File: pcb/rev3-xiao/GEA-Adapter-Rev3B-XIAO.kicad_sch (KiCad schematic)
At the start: 19 parts, among them J1 CURRENT_LIMITED_5V_IN, J2 GEA3_UART, U2 XIAO-ESP32-C3-SMD, U3 74LVC2G07

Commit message: feat(pcb): add rev3b appliance power path
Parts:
- removed J1: CURRENT_LIMITED_5V_IN, Connector_PinHeader_2.54mm:PinHeader_1x02_P2.54mm_Vertical, symbol Connector_Generic:Conn_01x02
- removed J2: GEA3_UART, Connector_PinHeader_2.54mm:PinHeader_1x02_P2.54mm_Vertical, symbol Connector_Generic:Conn_01x02
- added C10, C15: 100n 50V X7R, Capacitor_SMD:C_0603_1608Metric, symbol Device:C
- added C16, C17: 22u 16V X8L, Capacitor_SMD:C_1210_3225Metric, symbol Device:C
- added C8: 1u, Capacitor_SMD:C_0805_2012Metric, symbol Device:C
- added C9: 10u 50V X7R, Capacitor_SMD:C_1206_3216Metric, symbol Device:C
- added D12, D13: BZX84C12LT1G, Package_TO_SOT_SMD:SOT-23, symbol Diode:BZX84Cxx
- added D7: DNI, Diode_SMD:D_SMA, symbol Device:D_TVS
- added F1, F2: Polyfuse, Fuse:Fuse_1812_4532Metric, symbol Device:Polyfuse
- added J1: 8P8C, Connector_RJ:RJ45_Amphenol_54602-x08_Horizontal, symbol Connector:8P8C
- added JP2: APPLIANCE PIN 1 / PIN 3, Connector_PinHeader_2.54mm:PinHeader_1x03_P2.54mm_Vertical, symbol GEA:JP_PWR_3PIN
- added L1: 4.7uH, Inductor_SMD:L_Panasonic_PCC-M0530M, symbol Device:L
- added Q1, Q2: Si2309CDS, Package_TO_SOT_SMD:SOT-23, symbol Device:Q_PMOS_GSD
- added R30, R9: 9.1k, Resistor_SMD:R_0805_2012Metric, symbol Device:R
- added R8: DNP, Resistor_SMD:R_0805_2012Metric, symbol Device:R
- added U8: AP63205WU, Package_TO_SOT_SMD:TSOT-23-6, symbol Regulator_Switching:AP63205WU
- U2: LCSC/JLCPCB (none) -> C18212168
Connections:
- net APPL_5V: now also C16.1, C17.1, L1.2, U8.1 (FB)
- net GEA3_APPL_RX: now also J1.4
- net GEA3_APPL_TX: now also J1.5
- net GND: now also C10.1, C16.2, C17.2, C9.2, D7.1 (A1), J1.8, R30.2, R9.1, U8.4 (GND)
- new net ALT_PWR: F1.1, J1.3
- new net APPLIANCE_PROTECTED: C10.2, C9.1, Q2.3 (D), U8.2 (EN), U8.3 (IN)
- new net BUCK_BST: C15.1, U8.6 (BST)
- new net BUCK_SW: C15.2, L1.1, U8.5 (SW)
- new net PIN1_FUSED: F2.2, JP2.1 (RUN)
- new net PIN3_FUSED: F1.2, JP2.3 (NC_PARK)
- new net PWR_PROTECT_MID: C8.1, D12.3 (K), D13.3 (K), Q1.2 (S), Q2.2 (S), R8.2
- new net PWR_SELECTED: D7.2 (A2), JP2.2 (XIAO_5V), Q1.3 (D)
- new net Q1_GATE: D12.1 (A), Q1.1 (G), R30.1
- new net Q2_GATE: C8.2, D13.1 (A), Q2.1 (G), R8.1, R9.2
- new net VDC: F2.1, J1.1
- no-connect marks 16 -> 19
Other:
- note added: "JP2: appliance input selector. Shunt 1-2 selects RJ45 pin 1 VDC; shunt 2-3 selects pin 3 ALT_PWR. Move only with power off."
- note added: "JP_PWR is separate: RUN bridges appliance-regulated 5 V to XIAO VBUS; USB DEBUG parks the shunt and isolates appliance power."

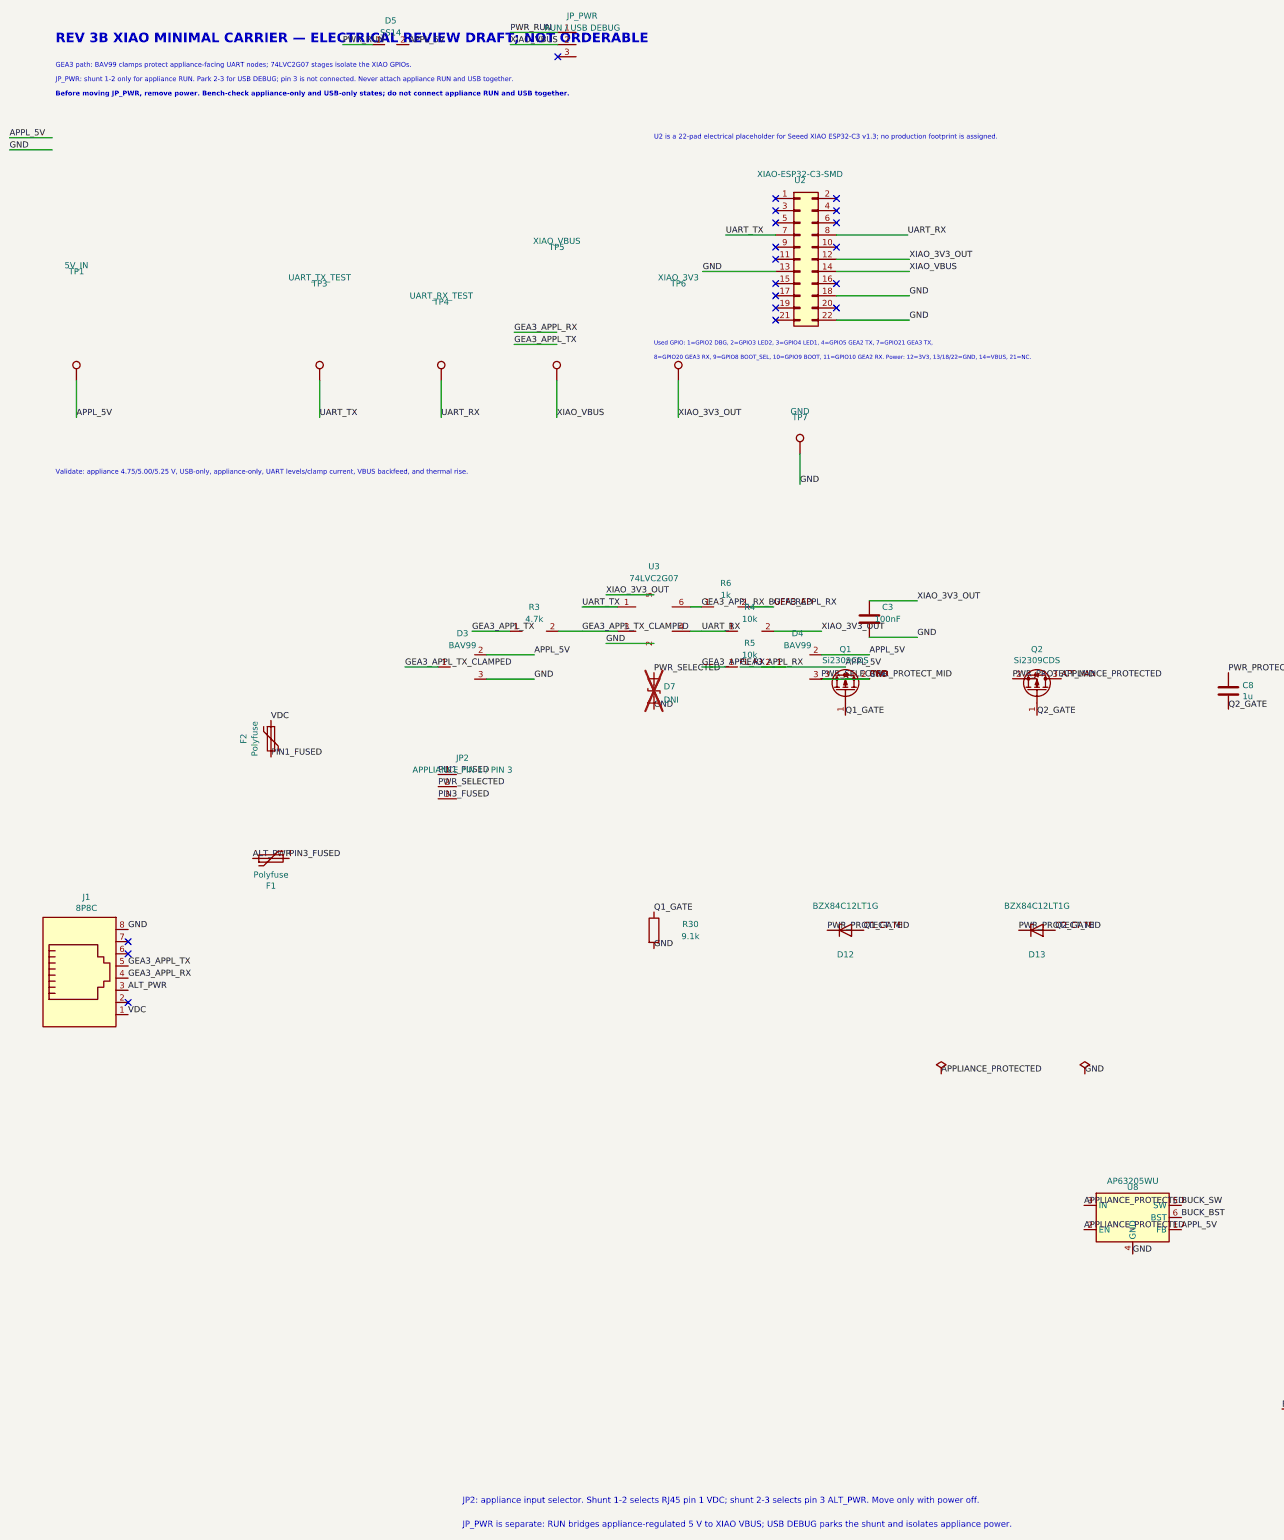
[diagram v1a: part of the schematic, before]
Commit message: fix(pcb): number rev3b power jumper
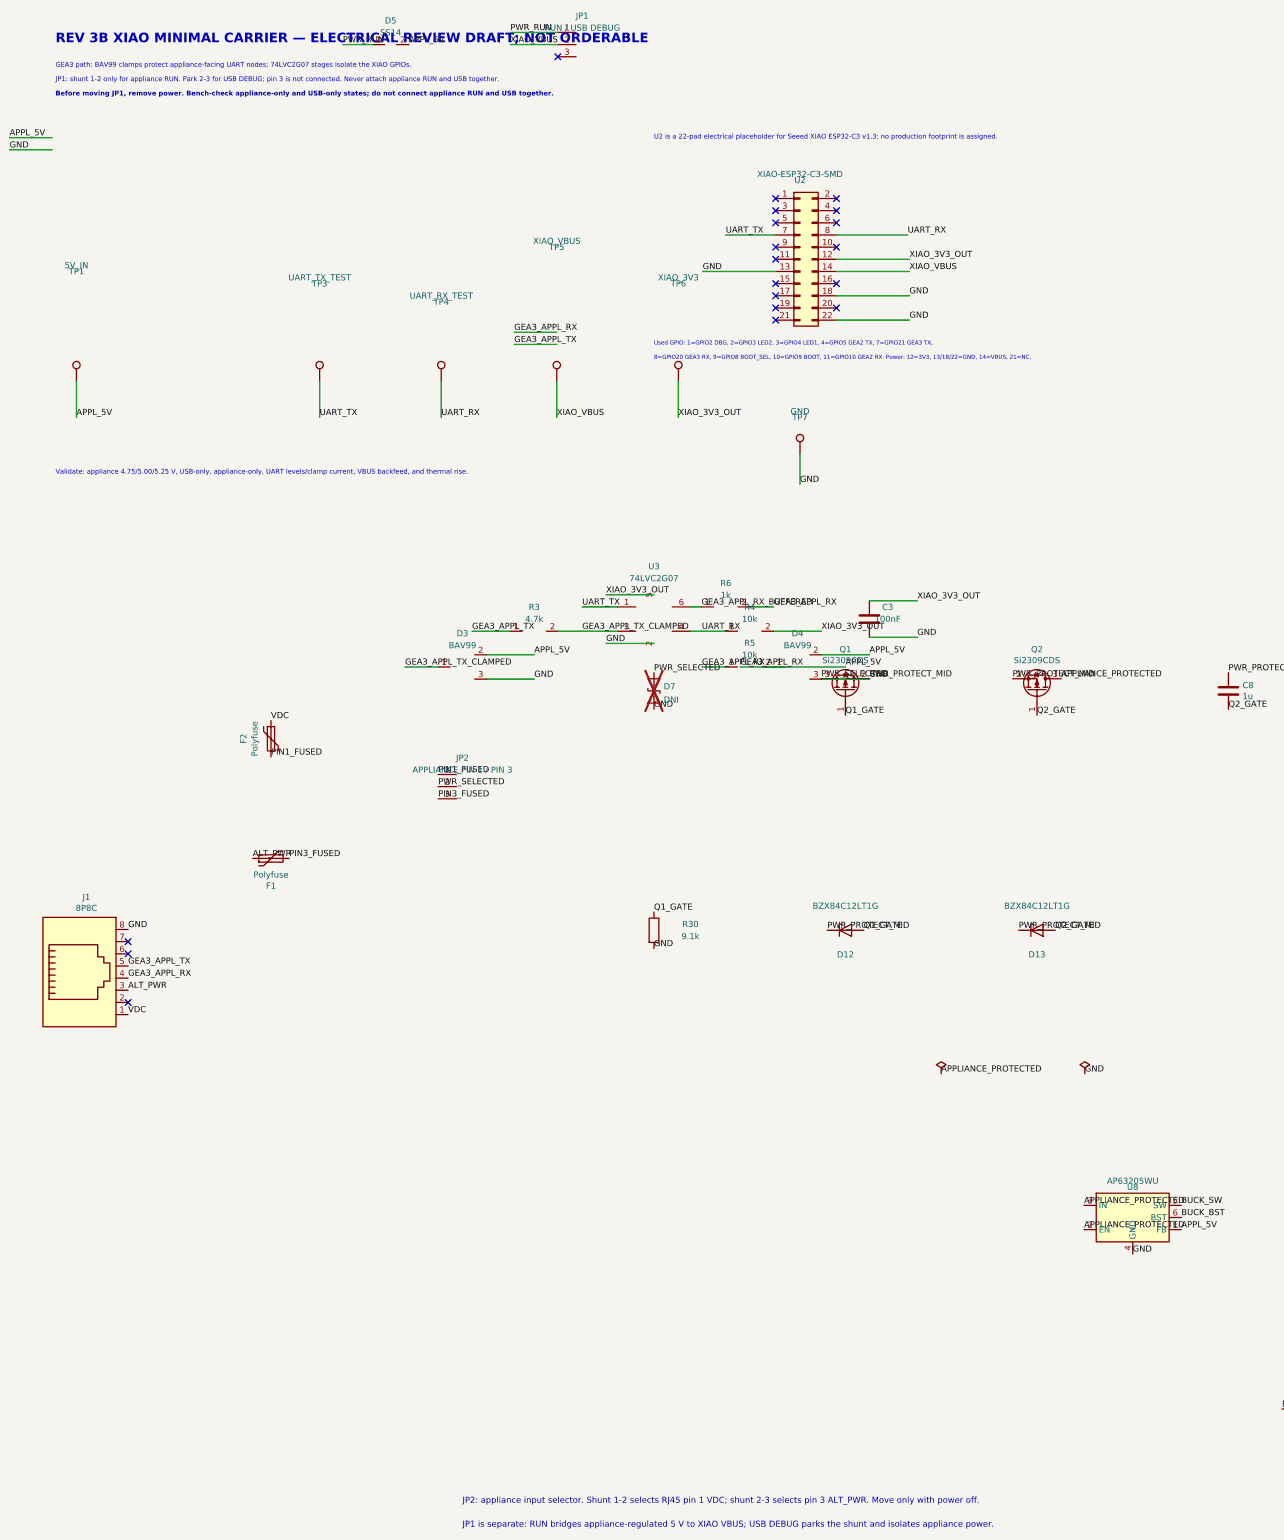
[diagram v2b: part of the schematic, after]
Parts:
- renumbered JP_PWR to JP1
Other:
- note added: "Before moving JP1, remove power. Bench-check appliance-only and USB-only states; do not connect appliance RUN and USB together."
- note added: "JP1 is separate: RUN bridges appliance-regulated 5 V to XIAO VBUS; USB DEBUG parks the shunt and isolates appliance power."
- note added: "JP1: shunt 1-2 only for appliance RUN. Park 2-3 for USB DEBUG; pin 3 is not connected. Never attach appliance RUN and USB together."
- note removed: "Before moving JP_PWR, remove power. Bench-check appliance-only and USB-only states; do not connect appliance RUN and USB together."
- note removed: "JP_PWR is separate: RUN bridges appliance-regulated 5 V to XIAO VBUS; USB DEBUG parks the shunt and isolates appliance power."
- note removed: "JP_PWR: shunt 1-2 only for appliance RUN. Park 2-3 for USB DEBUG; pin 3 is not connected. Never attach appliance RUN and USB together."
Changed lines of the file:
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@@
 		(on_board yes)
 		(dnp no)
-		(property "Reference" "JP_PWR" (at 145 19 0) (effects (font (size 1.27 1.27))))
+		(property "Reference" "JP1" (at 145 19 0) (effects (font (size 1.27 1.27))))
 		(property "Value" "RUN / USB DEBUG" (at 145 21.5 0) (effects (font (size 1.27 1.27))))
 		(property "Footprint" "Connector_PinHeader_2.54mm:PinHeader_1x03_P2.54mm_Vertical" (at 145 25 0) (effects (font (size 1.27 1.27)) (hide yes)))
@@
 		(pin "2")
 		(pin "3")
-		(instances (project "" (path "/64c3e063-c36f-4f7f-9f5c-b0c05a6486f2" (reference "JP_PWR") (unit 1))))
+		(instances (project "" (path "/64c3e063-c36f-4f7f-9f5c-b0c05a6486f2" (reference "JP1") (unit 1))))
 	)
 	(symbol
@@
 		)
 	)
-	(text "JP_PWR: shunt 1-2 only for appliance RUN. Park 2-3 for USB DEBUG; pin 3 is not connected. Never attach appliance RUN and USB together."
+	(text "JP1: shunt 1-2 only for appliance RUN. Park 2-3 for USB DEBUG; pin 3 is not connected. Never attach appliance RUN and USB together."
 		(exclude_from_sim no)
 		(at 35 33 0)
@@
 		)
 	)
-	(text "Before moving JP_PWR, remove power. Bench-check appliance-only and USB-only states; do not connect appliance RUN and USB together."
+	(text "Before moving JP1, remove power. Bench-check appliance-only and USB-only states; do not connect appliance RUN and USB together."
 		(exclude_from_sim no)
 		(at 35 36 0)
@@
 		(effects (font (size 1.27 1.27)) (justify left bottom))
 	)
-	(text "JP_PWR is separate: RUN bridges appliance-regulated 5 V to XIAO VBUS; USB DEBUG parks the shunt and isolates appliance power."
+	(text "JP1 is separate: RUN bridges appliance-regulated 5 V to XIAO VBUS; USB DEBUG parks the shunt and isolates appliance power."
 		(exclude_from_sim no)
 		(at 120 335 0)

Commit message: build(pcb): add rev3b supplier identifiers
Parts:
- U2: LCSC (none) -> C18212168; LCSC/JLCPCB C18212168 -> (none); MPN XIAO-ESP32-C3 -> 113991054
- U8: LCSC (none) -> C2071056
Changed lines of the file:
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@@
       (effects (font (size 1.27 1.27)) (hide yes))
     )
-    (property "MPN" "XIAO-ESP32-C3" (at 190.5 69.85 0)
+    (property "MPN" "113991054" (at 190.5 69.85 0)
       (effects (font (size 1.27 1.27)) (hide yes))
     )
-    (property "LCSC/JLCPCB" "C18212168" (at 190.5 69.85 0)
+    (property "LCSC" "C18212168" (at 190.5 69.85 0)
       (effects (font (size 1.27 1.27)) (hide yes))
     )
@@
 			(at 260.0000 270.0000 0)
 			(effects
+				(font
+					(size 1.27 1.27)
+				)
+				(hide yes)
+			)
+		)
+		(property "LCSC" "C2071056"
+			(at 260.0000 270.0000 0)
+			(effects
